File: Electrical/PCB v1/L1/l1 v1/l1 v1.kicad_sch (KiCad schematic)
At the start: 167 parts, among them J1 Conn_01x01_Socket, J2 Conn_01x01_Socket, SW1 SW_SPDT, U1 ESP32-S3-DEVKITM-1-N8, U2 LM2596ADJ

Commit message: errr new resources parts list
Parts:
- LED_1, LED_10, LED_11, LED_12, LED_13, LED_14, LED_15, LED_16, LED_17, LED_18, LED_19, LED_2, LED_20, LED_21, LED_22, LED_23, LED_24, LED_25, LED_26, LED_27, LED_28, LED_29, LED_3, LED_30, LED_31, LED_32, LED_4, LED_5, LED_6, LED_7, LED_8, LED_9: footprint (none) -> photoresistor:XDCR_ALS-PT19-315C_L177_TR8
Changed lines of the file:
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@@
 			)
 		)
-		(property "Footprint" ""
+		(property "Footprint" "photoresistor:XDCR_ALS-PT19-315C_L177_TR8"
 			(at 243.84 166.37 90)
 			(effects
@@
 			)
 		)
-		(property "Footprint" ""
+		(property "Footprint" "photoresistor:XDCR_ALS-PT19-315C_L177_TR8"
 			(at 243.84 168.91 90)
 			(effects
@@
 			)
 		)
-		(property "Footprint" ""
+		(property "Footprint" "photoresistor:XDCR_ALS-PT19-315C_L177_TR8"
 			(at 304.8 209.55 90)
 			(effects
@@
 			)
 		)
-		(property "Footprint" ""
+		(property "Footprint" "photoresistor:XDCR_ALS-PT19-315C_L177_TR8"
 			(at 304.8 212.09 90)
 			(effects
@@
 			)
 		)
-		(property "Footprint" ""
+		(property "Footprint" "photoresistor:XDCR_ALS-PT19-315C_L177_TR8"
 			(at 304.8 189.23 90)
 			(effects
@@
 			)
 		)
-		(property "Footprint" ""
+		(property "Footprint" "photoresistor:XDCR_ALS-PT19-315C_L177_TR8"
 			(at 304.8 191.77 90)
 			(effects
@@
 			)
 		)
-		(property "Footprint" ""
+		(property "Footprint" "photoresistor:XDCR_ALS-PT19-315C_L177_TR8"
 			(at 304.8 196.85 90)
 			(effects
@@
 			)
 		)
-		(property "Footprint" ""
+		(property "Footprint" "photoresistor:XDCR_ALS-PT19-315C_L177_TR8"
 			(at 304.8 207.01 90)
 			(effects
@@
 			)
 		)
-		(property "Footprint" ""
+		(property "Footprint" "photoresistor:XDCR_ALS-PT19-315C_L177_TR8"
 			(at 304.8 168.91 90)
 			(effects
@@
 			)
 		)
-		(property "Footprint" ""
+		(property "Footprint" "photoresistor:XDCR_ALS-PT19-315C_L177_TR8"
 			(at 243.84 184.15 90)
 			(effects
@@
 			)
 		)
-		(property "Footprint" ""
+		(property "Footprint" "photoresistor:XDCR_ALS-PT19-315C_L177_TR8"
 			(at 243.84 173.99 90)
 			(effects
@@
 			)
 		)
-		(property "Footprint" ""
+		(property "Footprint" "photoresistor:XDCR_ALS-PT19-315C_L177_TR8"
 			(at 304.8 204.47 90)
 			(effects
@@
 			)
 		)
-		(property "Footprint" ""
+		(property "Footprint" "photoresistor:XDCR_ALS-PT19-315C_L177_TR8"
 			(at 243.84 189.23 90)
 			(effects
@@
 			)
 		)
-		(property "Footprint" ""
+		(property "Footprint" "photoresistor:XDCR_ALS-PT19-315C_L177_TR8"
 			(at 243.84 181.61 90)
 			(effects
@@
 			)
 		)
-		(property "Footprint" ""
+		(property "Footprint" "photoresistor:XDCR_ALS-PT19-315C_L177_TR8"
 			(at 243.84 171.45 90)
 			(effects
@@
 			)
 		)
-		(property "Footprint" ""
+		(property "Footprint" "photoresistor:XDCR_ALS-PT19-315C_L177_TR8"
 			(at 304.8 166.37 90)
 			(effects
@@
 			)
 		)
-		(property "Footprint" ""
+		(property "Footprint" "photoresistor:XDCR_ALS-PT19-315C_L177_TR8"
 			(at 243.84 186.69 90)
 			(effects
@@
 			)
 		)
-		(property "Footprint" ""
+		(property "Footprint" "photoresistor:XDCR_ALS-PT19-315C_L177_TR8"
 			(at 304.8 184.15 90)
 			(effects
@@
 			)
 		)
-		(property "Footprint" ""
+		(property "Footprint" "photoresistor:XDCR_ALS-PT19-315C_L177_TR8"
 			(at 304.8 199.39 90)
 			(effects
@@
 			)
 		)
-		(property "Footprint" ""
+		(property "Footprint" "photoresistor:XDCR_ALS-PT19-315C_L177_TR8"
 			(at 304.8 173.99 90)
 			(effects
@@
 			)
 		)
-		(property "Footprint" ""
+		(property "Footprint" "photoresistor:XDCR_ALS-PT19-315C_L177_TR8"
 			(at 243.84 194.31 90)
 			(effects
@@
 			)
 		)
-		(property "Footprint" ""
+		(property "Footprint" "photoresistor:XDCR_ALS-PT19-315C_L177_TR8"
 			(at 304.8 194.31 90)
 			(effects
@@
 			)
 		)
-		(property "Footprint" ""
+		(property "Footprint" "photoresistor:XDCR_ALS-PT19-315C_L177_TR8"
 			(at 304.8 181.61 90)
 			(effects
@@
 			)
 		)
-		(property "Footprint" ""
+		(property "Footprint" "photoresistor:XDCR_ALS-PT19-315C_L177_TR8"
 			(at 304.8 186.69 90)
 			(effects
@@
 			)
 		)
-		(property "Footprint" ""
+		(property "Footprint" "photoresistor:XDCR_ALS-PT19-315C_L177_TR8"
 			(at 304.8 214.63 90)
 			(effects
@@
 			)
 		)
-		(property "Footprint" ""
+		(property "Footprint" "photoresistor:XDCR_ALS-PT19-315C_L177_TR8"
 			(at 304.8 179.07 90)
 			(effects
@@
 			)
 		)
-		(property "Footprint" ""
+		(property "Footprint" "photoresistor:XDCR_ALS-PT19-315C_L177_TR8"
 			(at 243.84 176.53 90)
 			(effects
@@
 			)
 		)
-		(property "Footprint" ""
+		(property "Footprint" "photoresistor:XDCR_ALS-PT19-315C_L177_TR8"
 			(at 304.8 176.53 90)
 			(effects
@@
 			)
 		)
-		(property "Footprint" ""
+		(property "Footprint" "photoresistor:XDCR_ALS-PT19-315C_L177_TR8"
 			(at 304.8 201.93 90)
 			(effects
@@
 			)
 		)
-		(property "Footprint" ""
+		(property "Footprint" "photoresistor:XDCR_ALS-PT19-315C_L177_TR8"
 			(at 243.84 179.07 90)
 			(effects
@@
 			)
 		)
-		(property "Footprint" ""
+		(property "Footprint" "photoresistor:XDCR_ALS-PT19-315C_L177_TR8"
 			(at 304.8 171.45 90)
 			(effects
@@
 			)
 		)
-		(property "Footprint" ""
+		(property "Footprint" "photoresistor:XDCR_ALS-PT19-315C_L177_TR8"
 			(at 243.84 191.77 90)
 			(effects

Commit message: mounting holes!
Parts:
- added H1, H10, H11, H12, H13, H14, H15, H16, H17, H18, H19, H2, H20, H21, H3, H4, H5, H6, H7, H8, H9: MountingHole, MountingHole:MountingHole_3.2mm_M3, symbol Mechanical:MountingHole
- LED1, LED10, LED11, LED12, LED13, LED14, LED15, LED16, LED17, LED18, LED19, LED2, LED20, LED21, LED22, LED23, LED24, LED25, LED26, LED27, LED28, LED29, LED3, LED30, LED31, LED32, LED4, LED5, LED6, LED7, LED8, LED9: footprint SM0603UYC:LED_SM0603UYC -> LED_SMD:LED_0201_0603Metric

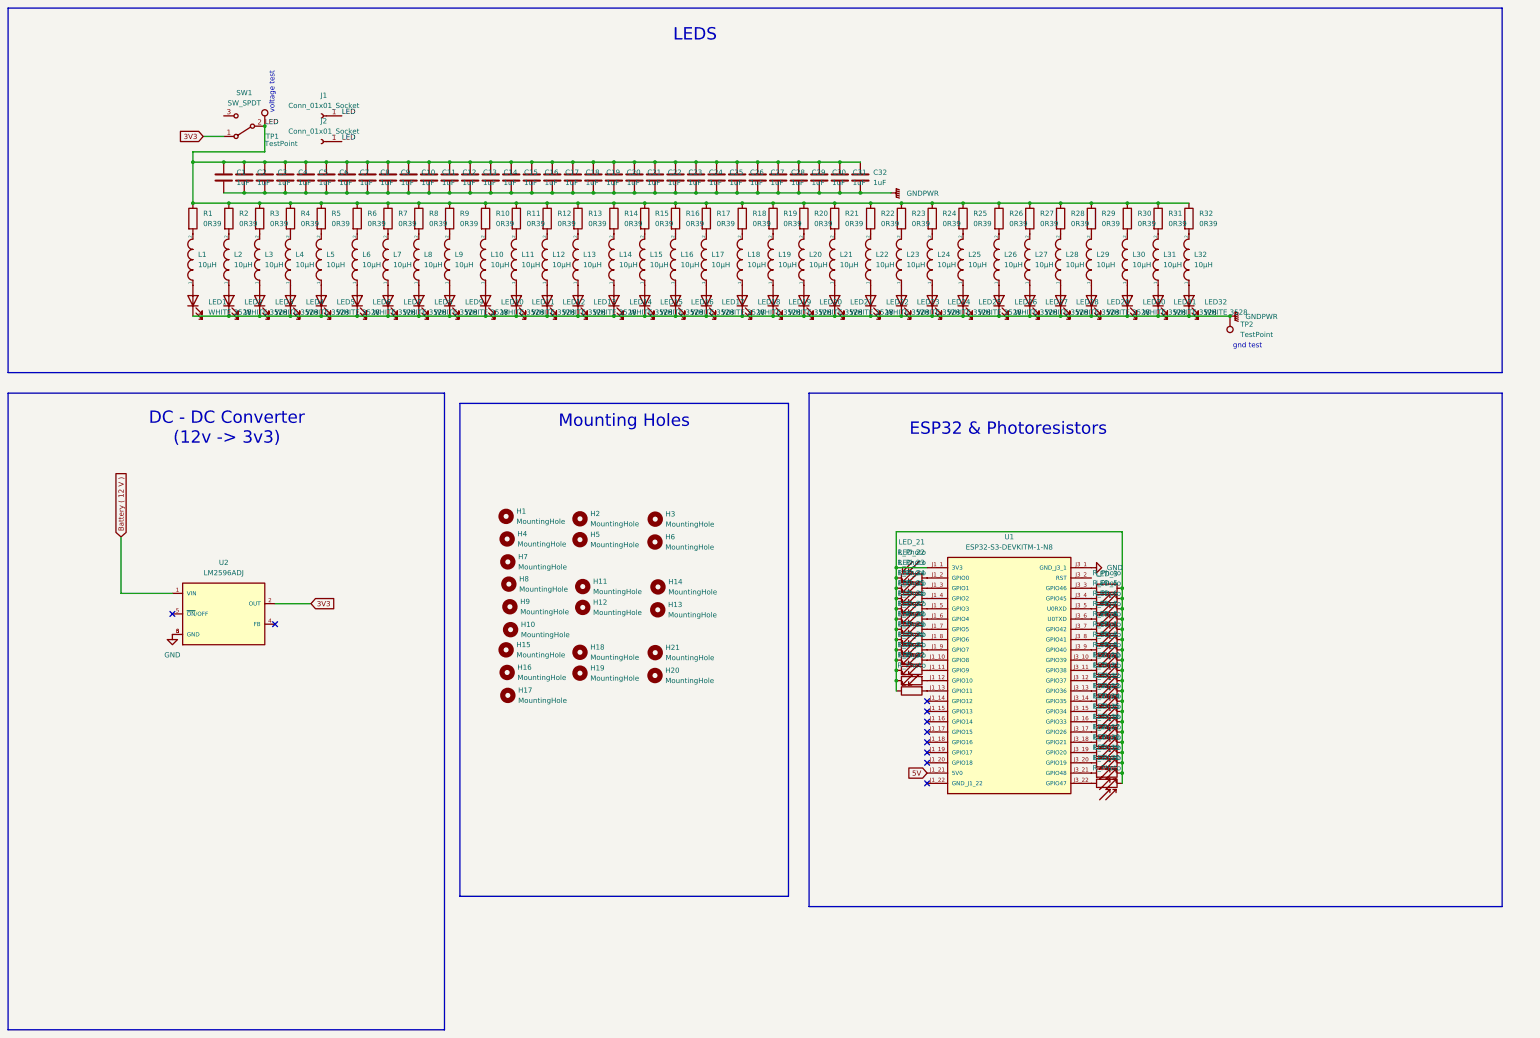
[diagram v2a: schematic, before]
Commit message: edge cuts xt 30 adn the essp 32 to be added
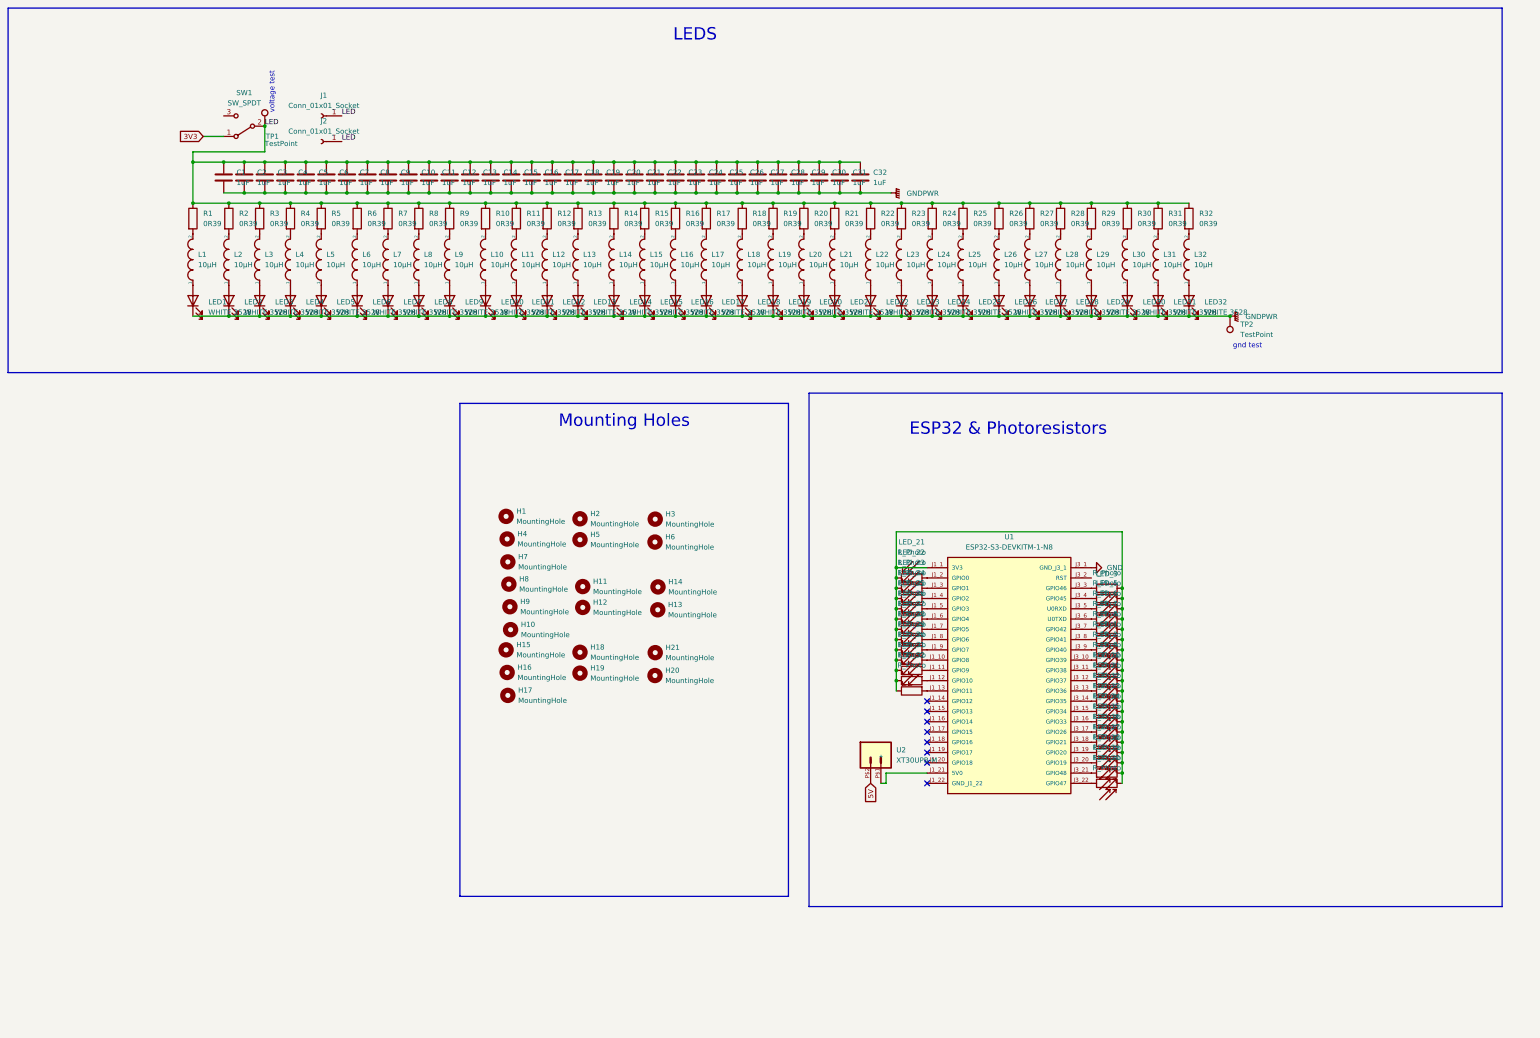
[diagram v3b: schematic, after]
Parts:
- removed U2: LM2596ADJ, LM2596ADJ:LM2596ADJ, symbol LM2596AD:LM2596ADJ
- added U2: XT30UPB-M, XT30UPB-M:XT30UPB-M, symbol amass xt 30:XT30UPB-M
- U1: footprint ESP32-S3-DEVKITM-1-N8:MODULE_ESP32-S3-DEVKITM-1-N8 -> ESP32 DEV KIT:MODULE_ESP32-S3-DEVKITM-1-N8
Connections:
- net 5V: now also U2.P$2 (-); no longer U1.J1_21 (5V0)
- new net: U1.J1_21 (5V0), U2.P$1 (+)
- no-connect marks 10 -> 8
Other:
- note removed: "DC - DC Converter (12v -> 3v3)"

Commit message: wired pcb minus esp 32 wiring
to be checked by haoyuan/haojun not done 100%
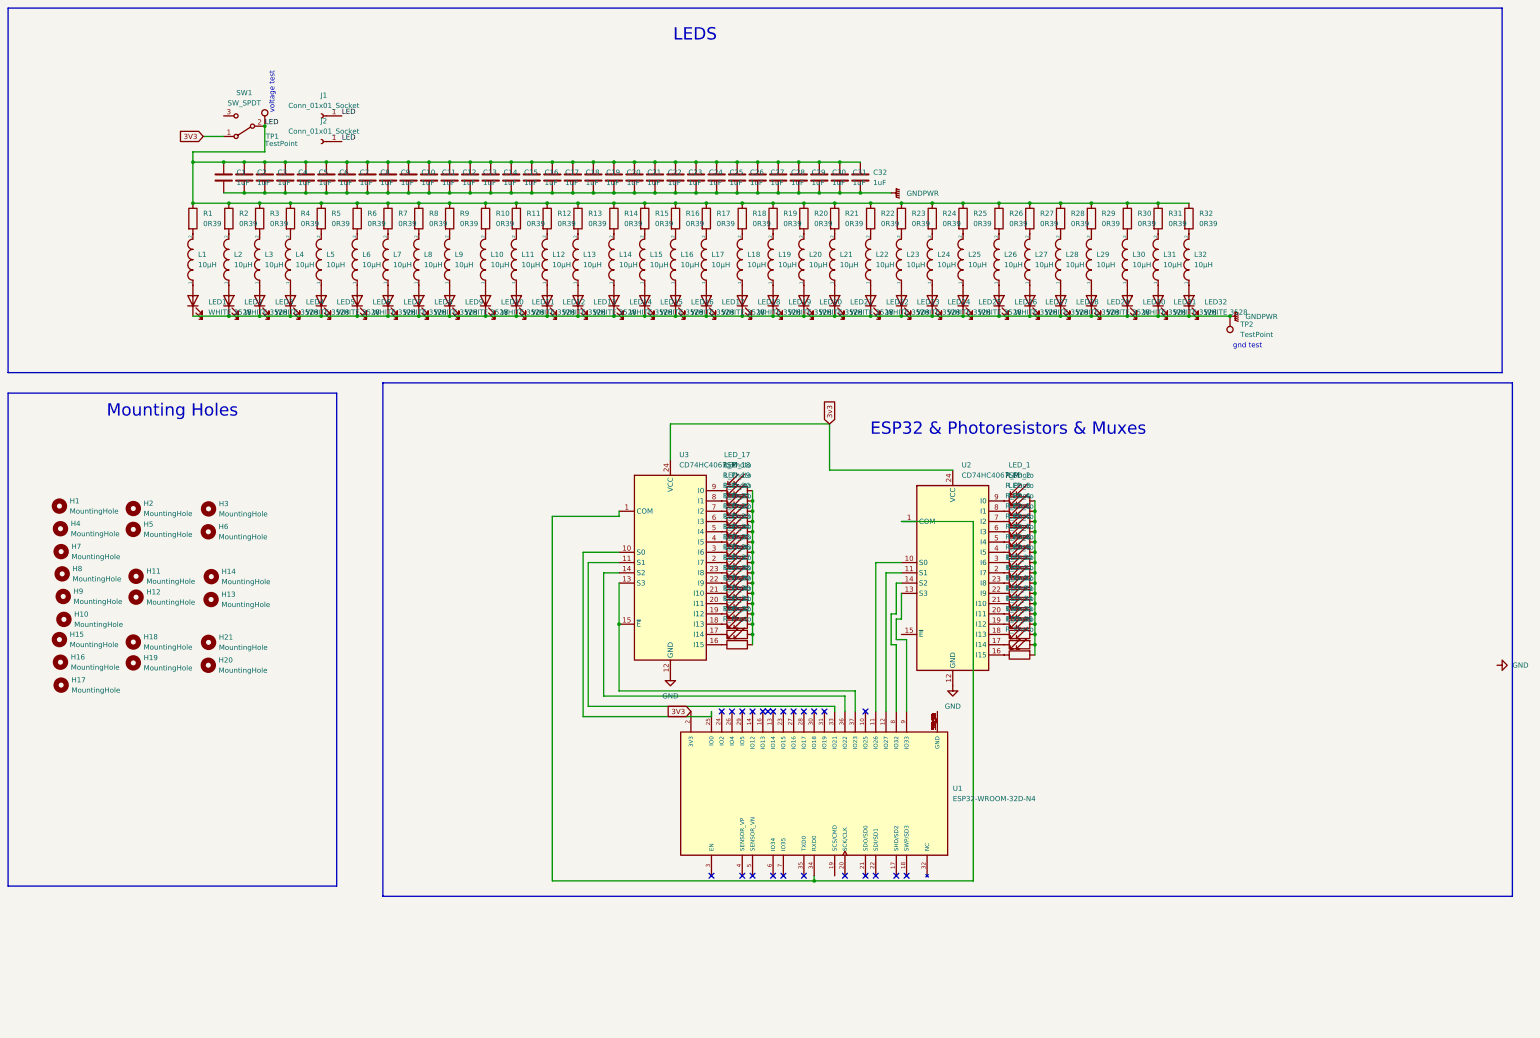
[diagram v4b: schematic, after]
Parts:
- removed U1: ESP32-S3-DEVKITM-1-N8, ESP32 DEV KIT:MODULE_ESP32-S3-DEVKITM-1-N8, symbol ESP32 DEV Kit:ESP32-S3-DEVKITM-1-N8
- removed U2: XT30UPB-M, XT30UPB-M:XT30UPB-M, symbol amass xt 30:XT30UPB-M
- added U1: ESP32-WROOM-32D-N4, esp32 thinfy:MODULE_ESP32-WROOM-32D-N4, symbol ESP32:ESP32-WROOM-32D-N4
- added U2, U3: CD74HC4067SM, mux thingy:SOP65P780X200-24N, symbol 74xx:CD74HC4067SM
- SW1: footprint Switches:SWITCH_SPDT_PTH_11.6X4.0MM -> Button_Switch_SMD:Nidec_Copal_CAS-120A
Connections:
- net 3V3: now also U1.2 (3V3)
- net GND: now also U2.12 (GND), U3.12 (GND)
- net at LED_21.1: now also LED_17.1, LED_18.1, LED_19.1, LED_20.1, LED_22.1, LED_23.1, LED_24.1, LED_25.1, LED_26.1, LED_27.1, LED_28.1, LED_29.1, LED_30.1, LED_31.1, LED_32.1
- net at LED_10.1: now also LED_1.1, LED_11.1, LED_12.1, LED_13.1, LED_14.1, LED_15.1, LED_16.1, LED_2.1, LED_3.1, LED_4.1, LED_5.1, LED_6.1, LED_7.1, LED_8.1, LED_9.1
- new net: LED_10.2, U2.22 (I9)
- new net: LED_20.2, U3.6 (I3)
- new net: U1.34 (RXD0), U2.1 (COM), U3.1 (COM)
- new net: U1.25 (IO0), U3.10 (S0)
- new net: U1.33 (IO21), U3.11 (S1)
- new net: U1.37 (IO23), U3.13 (S3), U3.15 (~{E})
- new net: U1.36 (IO22), U3.14 (S2)
- new net: LED_32.2, U3.16 (I15)
- new net: LED_31.2, U3.17 (I14)
- new net: LED_30.2, U3.18 (I13)
- new net: LED_29.2, U3.19 (I12)
- new net: LED_24.2, U3.2 (I7)
- new net: LED_28.2, U3.20 (I11)
- new net: LED_27.2, U3.21 (I10)
- new net: LED_26.2, U3.22 (I9)
- new net: LED_25.2, U3.23 (I8)
- new net: LED_23.2, U3.3 (I6)
- new net: LED_22.2, U3.4 (I5)
- new net: LED_21.2, U3.5 (I4)
- new net: LED_19.2, U3.7 (I2)
- new net: LED_18.2, U3.8 (I1)
- new net: LED_17.2, U3.9 (I0)
- new net: LED_14.2, U2.18 (I13)
- new net: LED_7.2, U2.3 (I6)
- new net: LED_9.2, U2.23 (I8)
- new net: LED_15.2, U2.17 (I14)
- new net: LED_12.2, U2.20 (I11)
- new net: LED_4.2, U2.6 (I3)
- new net: LED_6.2, U2.4 (I5)
- new net: LED_11.2, U2.21 (I10)
- new net: LED_3.2, U2.7 (I2)
- new net: LED_2.2, U2.8 (I1)
- new net: U1.11 (IO26), U2.10 (S0)
- new net: U1.12 (IO27), U2.11 (S1)
- new net: U1.9 (IO33), U2.13 (S3)
- new net: U1.8 (IO32), U2.14 (S2)
- new net: LED_16.2, U2.16 (I15)
- new net: LED_13.2, U2.19 (I12)
- new net: LED_8.2, U2.2 (I7)
- new net: LED_5.2, U2.5 (I4)
- new net: LED_1.2, U2.9 (I0)
- new net: U1.1 (GND), U1.15 (GND), U1.38 (GND), U1.39_1 (GND), U1.39_10 (GND), U1.39_11 (GND), U1.39_12 (GND), U1.39_13 (GND), U1.39_14 (GND), U1.39_15 (GND), U1.39_16 (GND), U1.39_17 (GND), U1.39_18 (GND), U1.39_19 (GND), U1.39_2 (GND), U1.39_20 (GND), U1.39_21 (GND), U1.39_3 (GND), U1.39_4 (GND), U1.39_5 (GND), U1.39_6 (GND), U1.39_7 (GND), U1.39_8 (GND), U1.39_9 (GND)
- new net 3v3: U2.24 (VCC), U3.24 (VCC)
- no-connect marks 8 -> 24
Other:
- note added: "ESP32 & Photoresistors & Muxes"
- note removed: "ESP32 & Photoresistors"
- moved on the sheet: H1, H10, H11, H12, H13, H14, H15, H16, H17, H18, H19, H2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

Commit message: gnd filled
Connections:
- net at U1.37 (IO23), U3.13 (S3): no longer U3.15 (~{E})
- no-connect marks 24 -> 25
